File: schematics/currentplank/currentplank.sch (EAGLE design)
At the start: 24 parts, among them IC1 74AHC1G86DBV, IC2 STCS2A, IC3 STCS2A

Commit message: Work on constant current plank.
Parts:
- removed SJ2, SJ3: (no value), jumper:SJ
- added IC4: OPAMP-DUALU, SparkFun-AnalogIC:OPAMP-DUALU
- added R6, R7: 1k, nickparts:TRIMPOT3MM-2
- R1, R3: value .1 ohm -> 0.05
- R2, R4: value .1 ohm -> 32k; device SparkFun-Passives:RESISTOR1206 -> SparkFun-Passives:RESISTOR0805-RES
- U$1: value LOKI_PLANKLONG -> LOKI_PLANKSHORT; device loki:LOKI_PLANKLONG -> loki:LOKI_PLANKSHORT
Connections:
- new net DISC2: IC3.DISC, U$1I1.2
- new net N$43: R2.1, R6.CW
- new net N$44: IC4B.+IN, R7.WIPER
- new net N$45: R4.1, R7.CW
- new net N$46: C2.1, C4.1, IC2.EN, IC2.VCC, IC3.EN, IC3.VCC, R5.1
- new net PWM2: IC3.PWM, U$1I1.1
- net +3V3: now also IC4A.V+, R2.2, R4.2
- net DISC1: now also U$1I2.2; no longer U$1I1.2
- net GND: now also IC4A.V-, R6.CCW, R7.CCW; no longer R2.2, R4.2
- net N$29: now also IC4A.-IN; no longer IC2.FB, SJ2.1
- net N$30: now also IC2.FB, IC4A.OUT; no longer R2.1, SJ2.2
- net N$33: now also D1.C, R5.2, SJ4.1; no longer D1.A, X1-1.KL
- net N$35: now also D1.A, X1-1.KL, X2-1.KL, X3-1.KL; no longer D1.C, R5.1, SJ4.1
- net N$36: now also IC4A.+IN, R6.WIPER; no longer C2.1, C4.1, IC2.EN, IC2.VCC, IC3.EN, IC3.VCC, R5.2, X2-2.KL, X3-2.KL
- net N$37: now also X2-2.KL; no longer X2-1.KL
- net N$38: now also X3-2.KL; no longer X3-1.KL
- net N$41: now also IC3.SOURCE, IC4B.-IN; no longer IC3.FB, SJ3.1
- net N$42: now also IC3.FB, IC4B.OUT; no longer R4.1, SJ3.2
- net PWM1: now also U$1I2.1; no longer U$1I1.1
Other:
- moved on the sheet: R1, R2, R3, R4, R5, SJ4, X2-1, X2-2, X3-1, X3-2

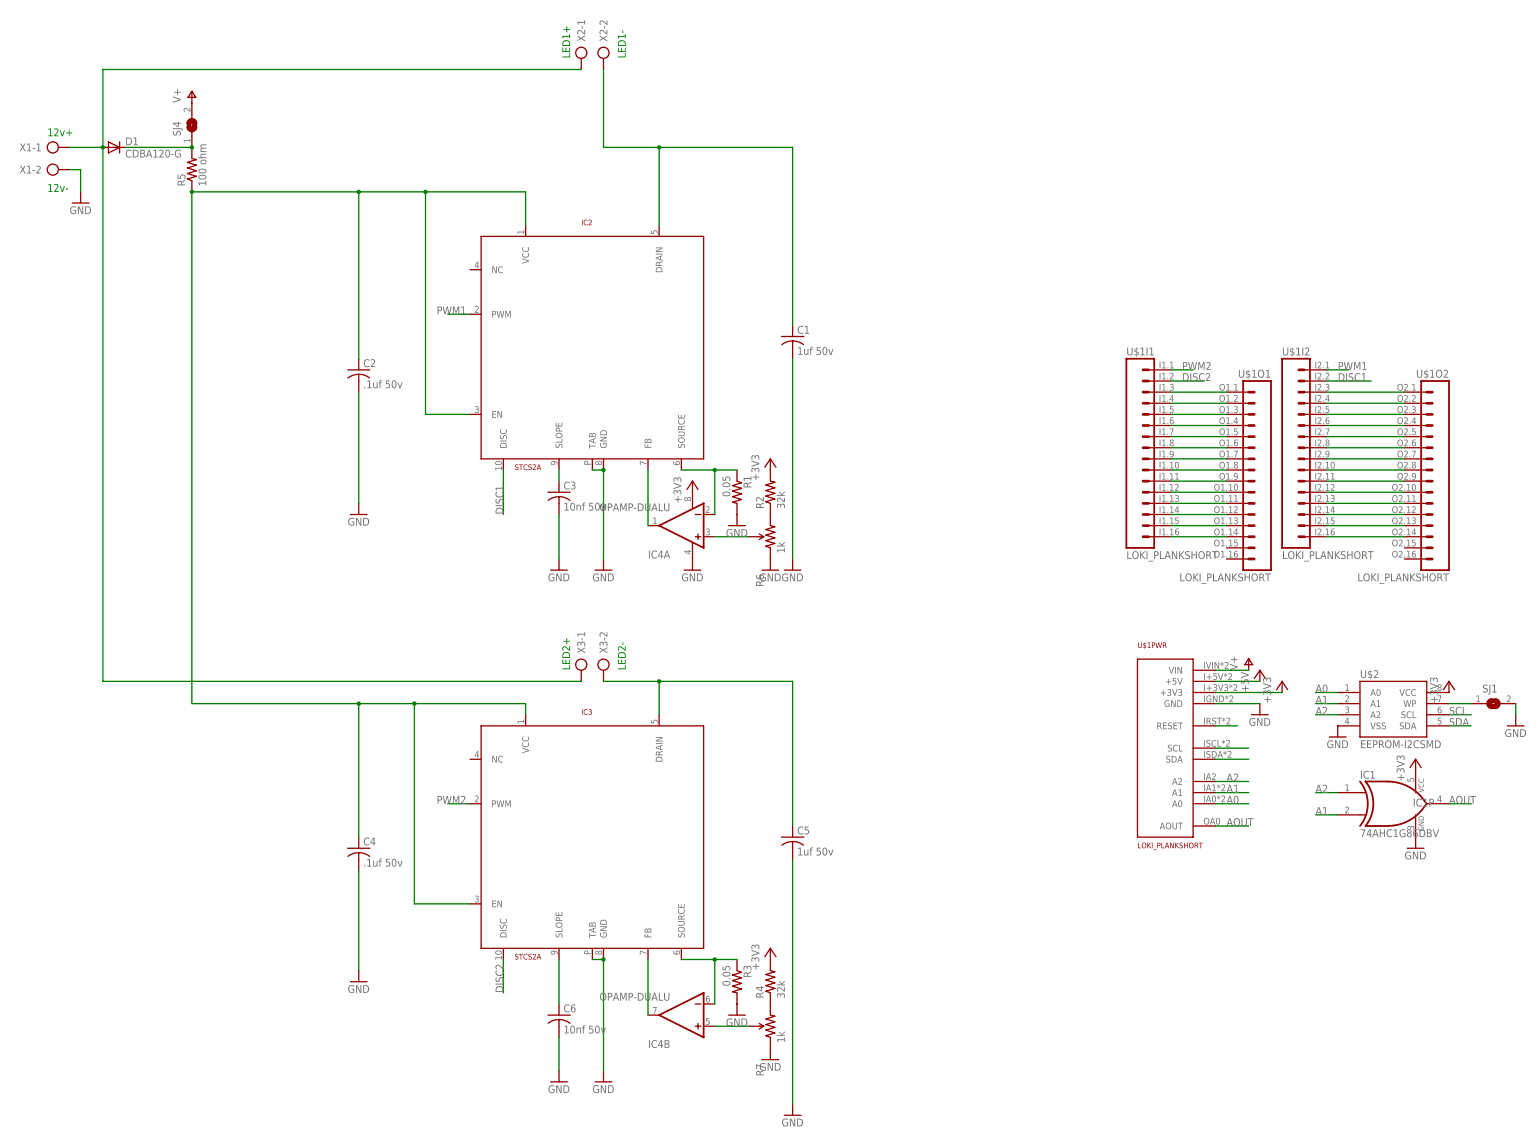
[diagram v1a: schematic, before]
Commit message: Rework of current plank, now using opamp and trimpot to set current limit.
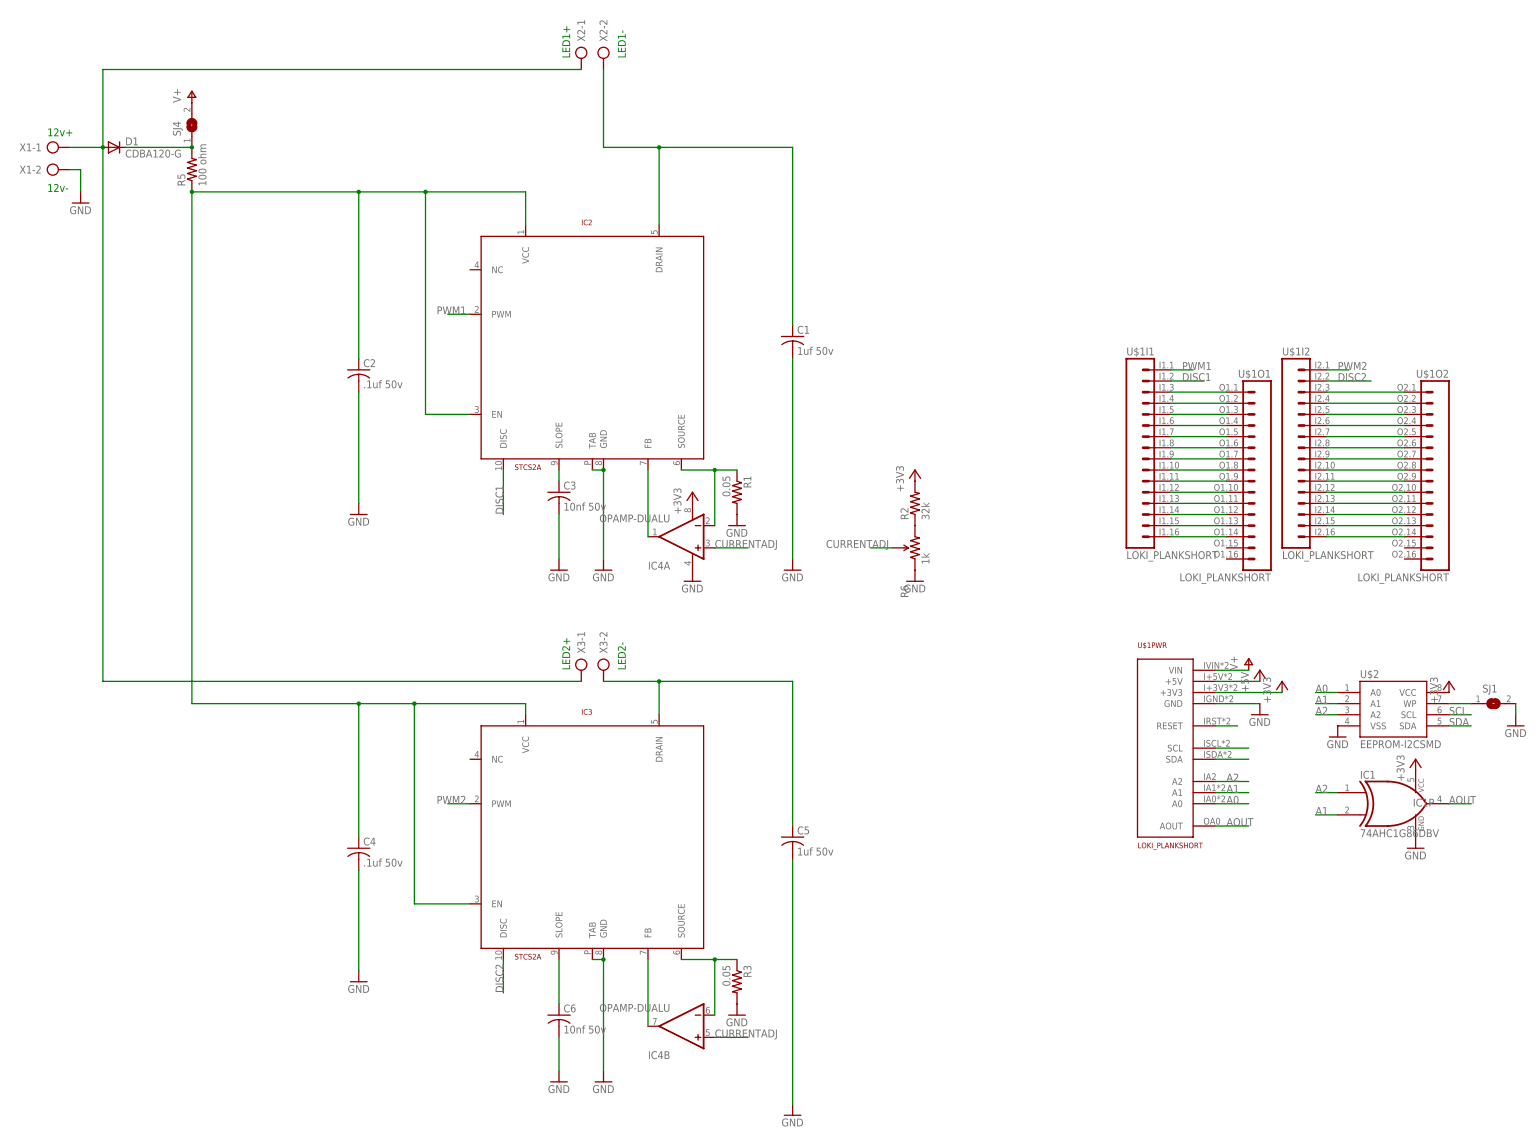
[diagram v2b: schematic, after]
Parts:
- removed R4: 32k, SparkFun-Passives:RESISTOR0805-RES
- removed R7: 1k, nickparts:TRIMPOT3MM-2
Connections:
- removed net N$36: IC4A.+IN, R6.WIPER
- removed net N$44: IC4B.+IN, R7.WIPER
- removed net N$45: R4.1, R7.CW
- new net CURRENTADJ: IC4A.+IN, IC4B.+IN, R6.WIPER
- net +3V3: no longer R4.2
- net DISC1: now also U$1I1.2; no longer U$1I2.2
- net DISC2: now also U$1I2.2; no longer U$1I1.2
- net GND: no longer R7.CCW
- net PWM1: now also U$1I1.1; no longer U$1I2.1
- net PWM2: now also U$1I2.1; no longer U$1I1.1
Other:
- moved on the sheet: IC4A, IC4B, R2, R6
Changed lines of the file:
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@@
 <part name="IC4" library="SparkFun-AnalogIC" deviceset="OPAMP-DUAL" device="U"/>
 <part name="R6" library="nickparts" deviceset="TRIMPOT" device="3MM-2" value="1k"/>
-<part name="R7" library="nickparts" deviceset="TRIMPOT" device="3MM-2" value="1k"/>
 <part name="GND6" library="supply1" deviceset="GND" device=""/>
 <part name="GND16" library="supply1" deviceset="GND" device=""/>
@@
 <part name="+3V5" library="supply1" deviceset="+3V3" device=""/>
 <part name="GND12" library="supply1" deviceset="GND" device=""/>
-<part name="GND18" library="supply1" deviceset="GND" device=""/>
-<part name="+3V6" library="supply1" deviceset="+3V3" device=""/>
-<part name="R4" library="SparkFun-Passives" deviceset="RESISTOR" device="0805-RES" value="32k"/>
 </parts>
 <sheets>
@@
 <instance part="P+3" gate="1" x="-215.9" y="170.18"/>
 <instance part="SJ4" gate="1" x="-215.9" y="162.56" rot="R90"/>
-<instance part="IC4" gate="A" x="-101.6" y="71.12" rot="MR0"/>
-<instance part="IC4" gate="B" x="-104.14" y="-40.64" rot="R180"/>
-<instance part="R6" gate="R?" x="-83.82" y="68.58" rot="R90"/>
-<instance part="R7" gate="R?" x="-83.82" y="-43.18" rot="R90"/>
-<instance part="GND6" gate="1" x="-101.6" y="60.96"/>
+<instance part="IC4" gate="A" x="-101.6" y="68.58" rot="MR0"/>
+<instance part="IC4" gate="B" x="-104.14" y="-43.18" rot="R180"/>
+<instance part="R6" gate="R?" x="-50.8" y="66.04" rot="R90"/>
+<instance part="GND6" gate="1" x="-101.6" y="58.42"/>
 <instance part="GND16" gate="1" x="-91.44" y="71.12"/>
-<instance part="+3V4" gate="G$1" x="-101.6" y="81.28"/>
-<instance part="GND17" gate="1" x="-83.82" y="60.96"/>
-<instance part="R2" gate="G$1" x="-83.82" y="78.74" rot="R90"/>
-<instance part="+3V5" gate="G$1" x="-83.82" y="86.36"/>
+<instance part="+3V4" gate="G$1" x="-101.6" y="78.74"/>
+<instance part="GND17" gate="1" x="-50.8" y="58.42"/>
+<instance part="R2" gate="G$1" x="-50.8" y="76.2" rot="R90"/>
+<instance part="+3V5" gate="G$1" x="-50.8" y="83.82"/>
 <instance part="GND12" gate="1" x="-91.44" y="-40.64"/>
-<instance part="GND18" gate="1" x="-83.82" y="-50.8"/>
-<instance part="+3V6" gate="G$1" x="-83.82" y="-25.4"/>
-<instance part="R4" gate="G$1" x="-83.82" y="-33.02" rot="R90"/>
 </instances>
 <busses>
@@
 <pinref part="R2" gate="G$1" pin="2"/>
 <pinref part="+3V5" gate="G$1" pin="+3V3"/>
-</segment>
-<segment>
-<pinref part="R4" gate="G$1" pin="2"/>
-<pinref part="+3V6" gate="G$1" pin="+3V3"/>
 </segment>
 </net>
@@
 <pinref part="R3" gate="G$1" pin="2"/>
 <pinref part="GND12" gate="1" pin="GND"/>
-</segment>
-<segment>
-<pinref part="R7" gate="R?" pin="CCW"/>
-<pinref part="GND18" gate="1" pin="GND"/>
 </segment>
 </net>
@@
 </segment>
 <segment>
-<pinref part="U$1" gate="I2" pin="1"/>
-<wire x1="43.18" y1="106.68" x2="48.26" y2="106.68" width="0.1524" layer="91"/>
-<label x="45.72" y="106.68" size="1.778" layer="95"/>
+<pinref part="U$1" gate="I1" pin="1"/>
+<wire x1="7.62" y1="106.68" x2="12.7" y2="106.68" width="0.1524" layer="91"/>
+<label x="10.16" y="106.68" size="1.778" layer="95"/>
 </segment>
 </net>
@@
 </segment>
 <segment>
-<pinref part="U$1" gate="I1" pin="1"/>
-<wire x1="7.62" y1="106.68" x2="12.7" y2="106.68" width="0.1524" layer="91"/>
-<label x="10.16" y="106.68" size="1.778" layer="95"/>
+<pinref part="U$1" gate="I2" pin="1"/>
+<wire x1="43.18" y1="106.68" x2="48.26" y2="106.68" width="0.1524" layer="91"/>
+<label x="45.72" y="106.68" size="1.778" layer="95"/>
 </segment>
 </net>
@@
 </segment>
 <segment>
+<pinref part="U$1" gate="I2" pin="2"/>
+<wire x1="43.18" y1="104.14" x2="53.34" y2="104.14" width="0.1524" layer="91"/>
+<label x="45.72" y="104.14" size="1.778" layer="95"/>
+</segment>
+</net>
+<net name="DISC1" class="0">
+<segment>
+<pinref part="IC2" gate="G$1" pin="DISC"/>
+<wire x1="-144.78" y1="83.82" x2="-144.78" y2="73.66" width="0.1524" layer="91"/>
+<label x="-144.78" y="73.66" size="1.778" layer="95" rot="R90"/>
+</segment>
+<segment>
 <pinref part="U$1" gate="I1" pin="2"/>
 <wire x1="7.62" y1="104.14" x2="15.24" y2="104.14" width="0.1524" layer="91"/>
 <label x="10.16" y="104.14" size="1.778" layer="95"/>
-</segment>
-</net>
-<net name="DISC1" class="0">
-<segment>
-<pinref part="IC2" gate="G$1" pin="DISC"/>
-<wire x1="-144.78" y1="83.82" x2="-144.78" y2="73.66" width="0.1524" layer="91"/>
-<label x="-144.78" y="73.66" size="1.778" layer="95" rot="R90"/>
-</segment>
-<segment>
-<pinref part="U$1" gate="I2" pin="2"/>
-<wire x1="43.18" y1="104.14" x2="53.34" y2="104.14" width="0.1524" layer="91"/>
-<label x="45.72" y="104.14" size="1.778" layer="95"/>
 </segment>
 </net>
@@
 <pinref part="IC4" gate="A" pin="-IN"/>
 <wire x1="-96.52" y1="83.82" x2="-104.14" y2="83.82" width="0.1524" layer="91"/>
-<wire x1="-96.52" y1="73.66" x2="-96.52" y2="83.82" width="0.1524" layer="91"/>
+<wire x1="-96.52" y1="71.12" x2="-96.52" y2="83.82" width="0.1524" layer="91"/>
 <junction x="-96.52" y="83.82"/>
 </segment>
@@
 <pinref part="IC4" gate="A" pin="OUT"/>
 <pinref part="IC2" gate="G$1" pin="FB"/>
-<wire x1="-111.76" y1="71.12" x2="-111.76" y2="83.82" width="0.1524" layer="91"/>
-</segment>
-</net>
-<net name="N$36" class="0">
-<segment>
-<pinref part="IC4" gate="A" pin="+IN"/>
-<pinref part="R6" gate="R?" pin="WIPER"/>
-<wire x1="-96.52" y1="68.58" x2="-88.9" y2="68.58" width="0.1524" layer="91"/>
+<wire x1="-111.76" y1="68.58" x2="-111.76" y2="83.82" width="0.1524" layer="91"/>
 </segment>
 </net>
@@
 <segment>
 <pinref part="IC4" gate="B" pin="-IN"/>
-<wire x1="-96.52" y1="-38.1" x2="-96.52" y2="-27.94" width="0.1524" layer="91"/>
+<wire x1="-96.52" y1="-40.64" x2="-96.52" y2="-27.94" width="0.1524" layer="91"/>
 <pinref part="IC3" gate="G$1" pin="SOURCE"/>
 <wire x1="-96.52" y1="-27.94" x2="-104.14" y2="-27.94" width="0.1524" layer="91"/>
@@
 <pinref part="IC4" gate="B" pin="OUT"/>
 <pinref part="IC3" gate="G$1" pin="FB"/>
-<wire x1="-111.76" y1="-40.64" x2="-111.76" y2="-27.94" width="0.1524" layer="91"/>
-</segment>
-</net>
-<net name="N$44" class="0">
+<wire x1="-111.76" y1="-43.18" x2="-111.76" y2="-27.94" width="0.1524" layer="91"/>
+</segment>
+</net>
+<net name="CURRENTADJ" class="0">
 <segment>
 <pinref part="IC4" gate="B" pin="+IN"/>
-<pinref part="R7" gate="R?" pin="WIPER"/>
-<wire x1="-96.52" y1="-43.18" x2="-88.9" y2="-43.18" width="0.1524" layer="91"/>
-</segment>
-</net>
-<net name="N$45" class="0">
-<segment>
-<pinref part="R7" gate="R?" pin="CW"/>
-<pinref part="R4" gate="G$1" pin="1"/>
-</segment>
-</net>
+<wire x1="-96.52" y1="-45.72" x2="-88.9" y2="-45.72" width="0.1524" layer="91"/>
+<label x="-96.52" y="-45.72" size="1.778" layer="95"/>
+</segment>
+<segment>
+<pinref part="IC4" gate="A" pin="+IN"/>
+<wire x1="-96.52" y1="66.04" x2="-88.9" y2="66.04" width="0.1524" layer="91"/>
+<label x="-96.52" y="66.04" size="1.778" layer="95"/>
+</segment>
+<segment>
+<pinref part="R6" gate="R?" pin="WIPER"/>
+<wire x1="-55.88" y1="66.04" x2="-60.96" y2="66.04" width="0.1524" layer="91"/>
+<label x="-71.12" y="66.04" size="1.778" layer="95"/>
+</segment>
+</net>

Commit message: Thermal vias etc for current plank.
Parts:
- IC2, IC3: device stcs2a:STCS2A -> currentplank:STCS2A_STCS2A
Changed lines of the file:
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@@
 <part name="SJ1" library="jumper" deviceset="SJ" device=""/>
 <part name="GND4" library="supply1" deviceset="GND" device=""/>
-<part name="IC2" library="stcs2a" deviceset="STCS2A" device="" value="STCS2A"/>
-<part name="IC3" library="stcs2a" deviceset="STCS2A" device="" value="STCS2A"/>
+<part name="IC2" library="currentplank" deviceset="STCS2A_STCS2A" device="" value="STCS2A"/>
+<part name="IC3" library="currentplank" deviceset="STCS2A_STCS2A" device="" value="STCS2A"/>
 <part name="C1" library="resistor" deviceset="C-US" device="C0805" value="1uf 50v"/>
 <part name="C2" library="resistor" deviceset="C-US" device="C0805" value=".1uf 50v"/>

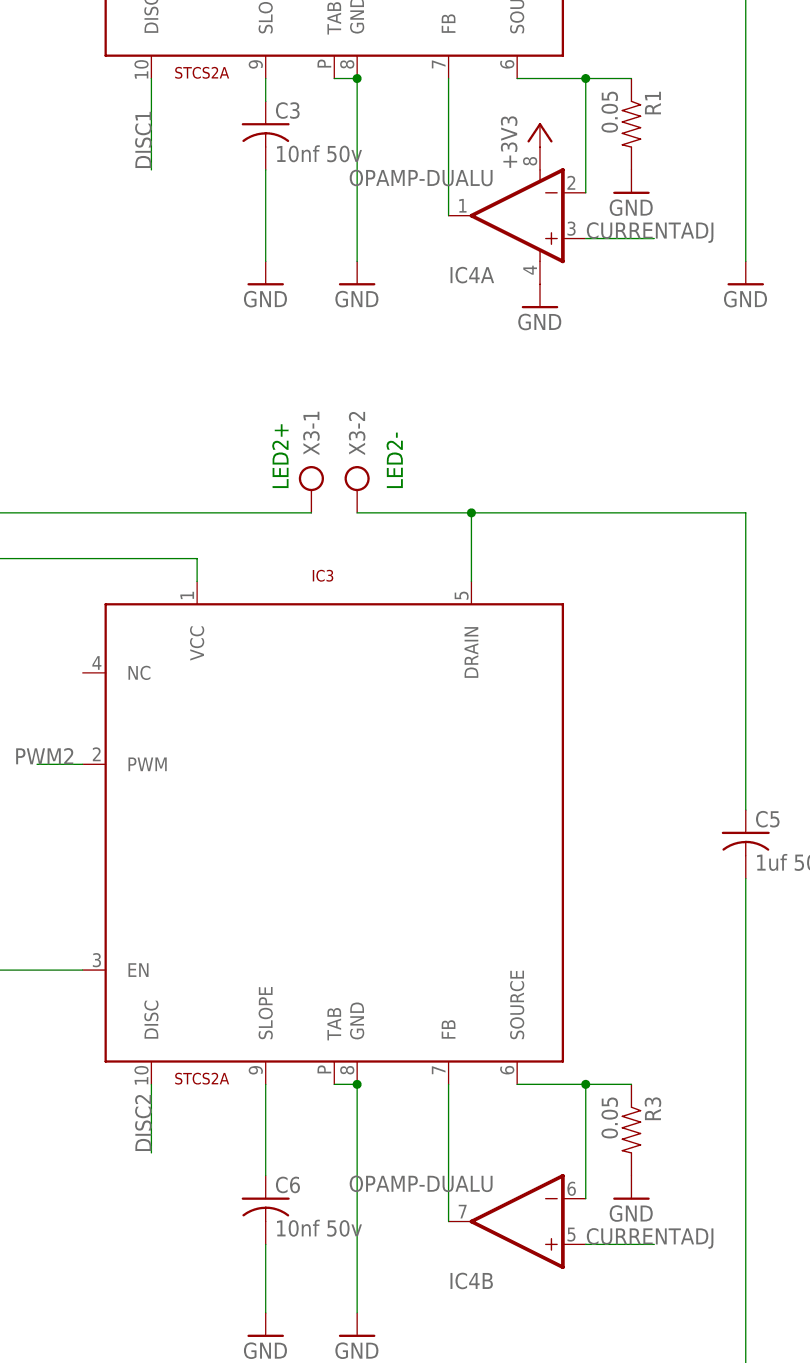
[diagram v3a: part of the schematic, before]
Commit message: Updates to current plank silkscreen etc.
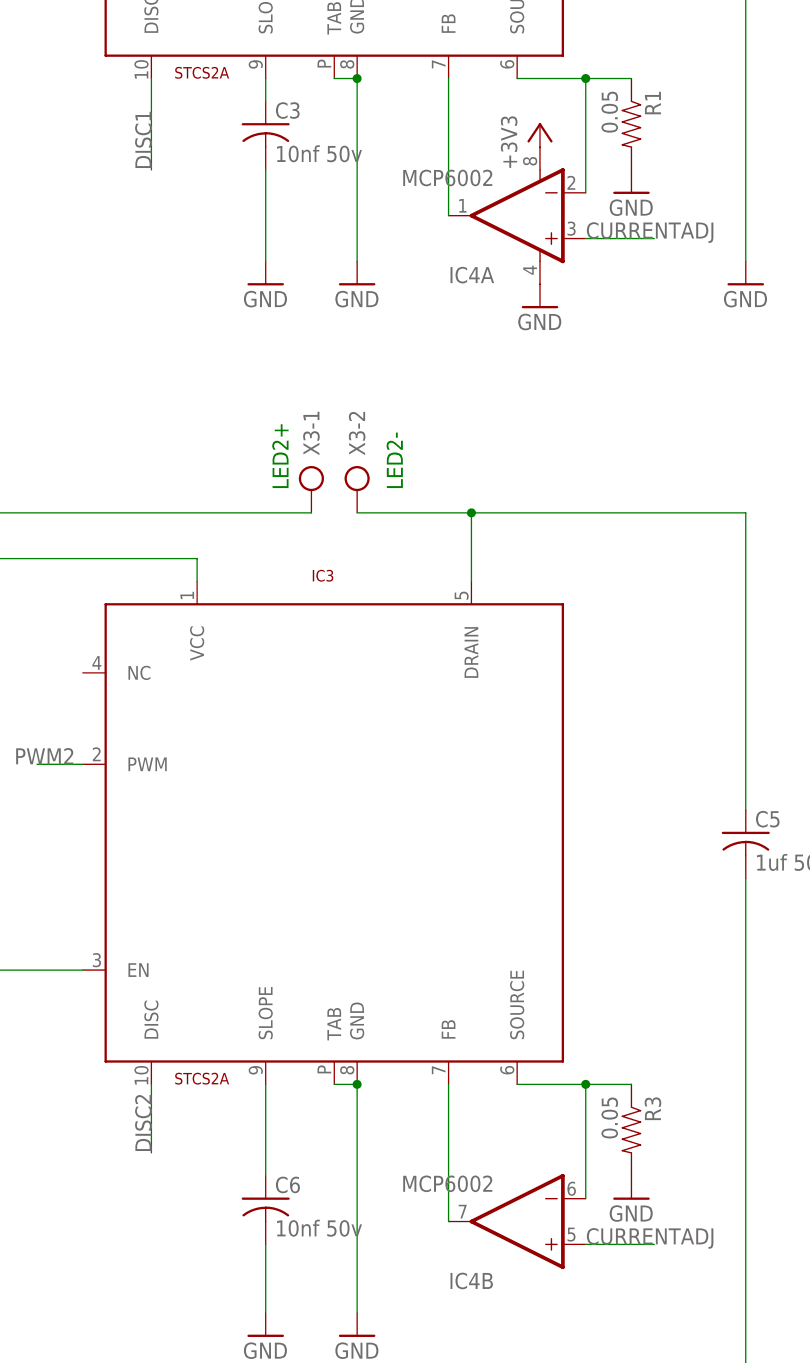
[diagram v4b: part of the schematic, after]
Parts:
- IC4: value OPAMP-DUALU -> MCP6002
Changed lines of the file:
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@@
 <part name="P+3" library="supply1" deviceset="V+" device=""/>
 <part name="SJ4" library="jumper" deviceset="SJ" device=""/>
-<part name="IC4" library="SparkFun-AnalogIC" deviceset="OPAMP-DUAL" device="U"/>
+<part name="IC4" library="SparkFun-AnalogIC" deviceset="OPAMP-DUAL" device="U" value="MCP6002"/>
 <part name="R6" library="nickparts" deviceset="TRIMPOT" device="3MM-2" value="1k"/>
 <part name="GND6" library="supply1" deviceset="GND" device=""/>
